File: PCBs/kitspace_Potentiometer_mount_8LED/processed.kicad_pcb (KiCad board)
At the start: 2 copper layers, 80 x 40 mm, 11 parts

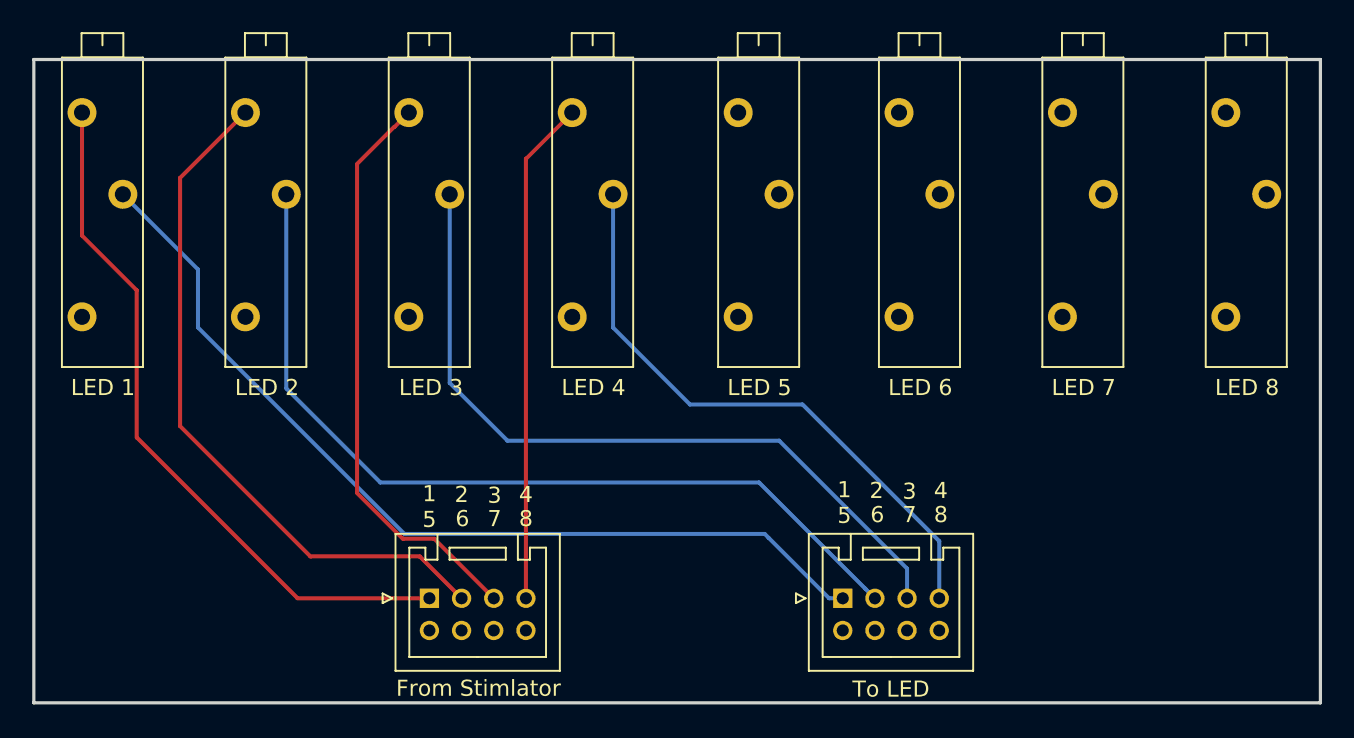
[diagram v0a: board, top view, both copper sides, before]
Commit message: recheck all circuits and clean up fill zone by rerouting the nets using freerouting and manually
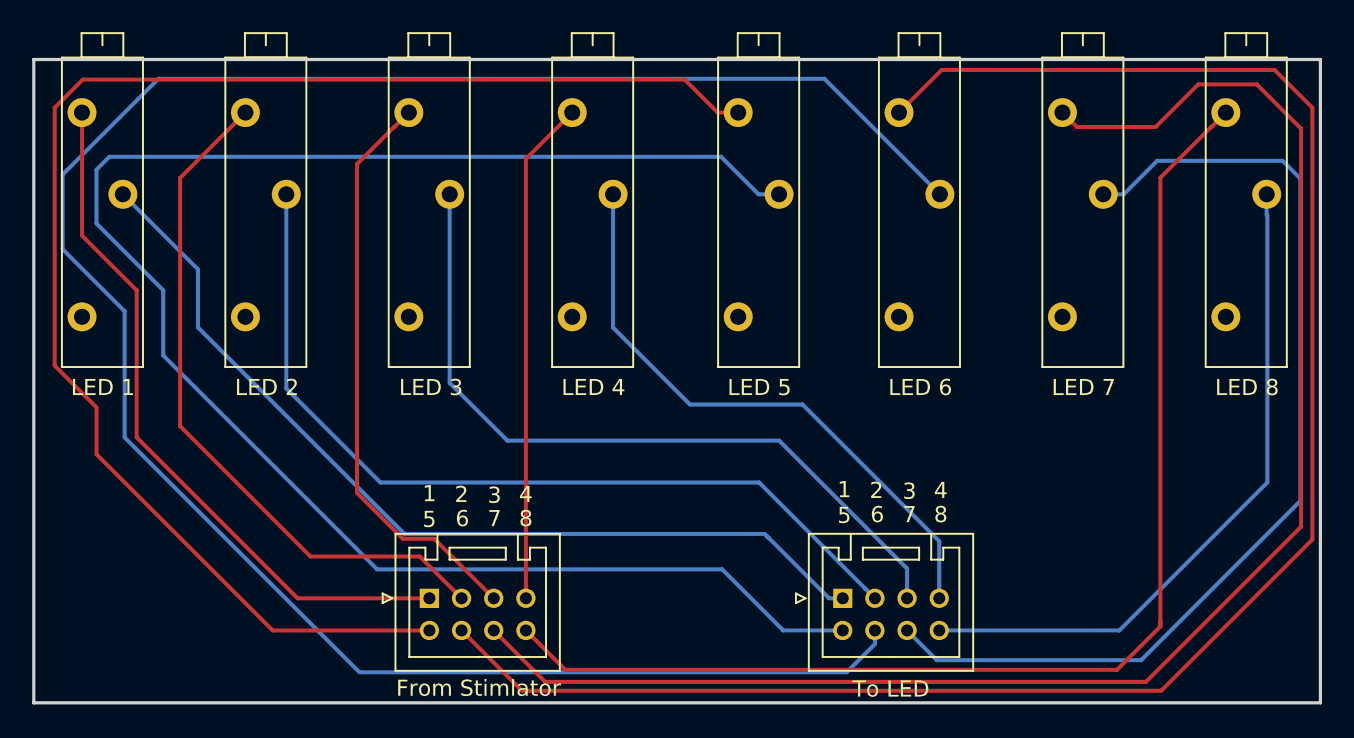
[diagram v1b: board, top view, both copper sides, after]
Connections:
- LED 1 pad 1: (no net) -> Net-(RV1-Pad1)
- LED 2 pad 1: (no net) -> Net-(RV2-Pad1)
- LED 3 pad 1: (no net) -> Net-(RV3-Pad1)
- LED 4 pad 1: (no net) -> Net-(RV4-Pad1)
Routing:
- net (no net): track 0.00 -> 721.7 mm
